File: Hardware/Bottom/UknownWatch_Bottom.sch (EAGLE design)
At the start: 32 parts, among them U1 AD5242-SO16

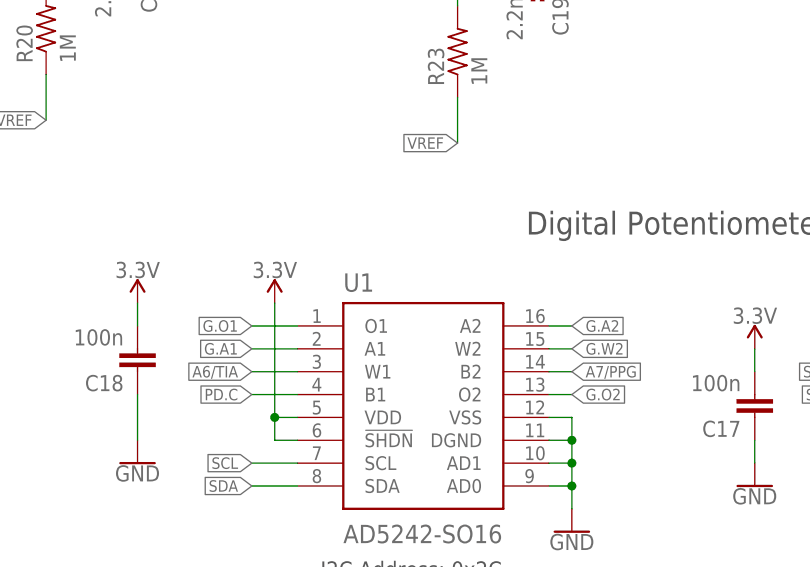
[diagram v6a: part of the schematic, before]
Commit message: Finished bulk of routing on bottom board
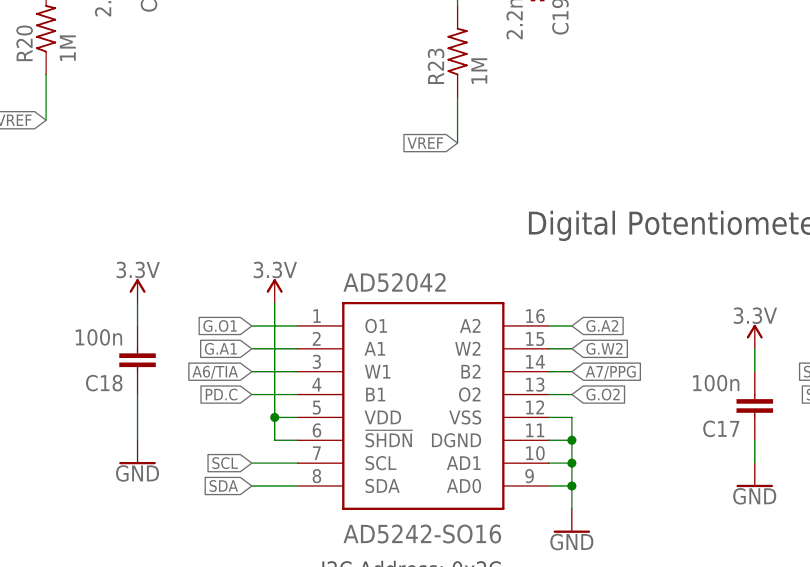
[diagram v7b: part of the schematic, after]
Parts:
- renumbered U1 to AD52042
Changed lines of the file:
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@@
 <part name="GND22" library="LinnesLab-Symbols" deviceset="GND" device=""/>
 <part name="SUPPLY16" library="LinnesLab-Symbols" deviceset="3.3V" device=""/>
-<part name="U1" library="LinnesLab-DigitalIC" deviceset="AD5242" device="-SO16" package3d_urn="urn:adsk.eagle:package:16423/2"/>
+<part name="AD52042" library="LinnesLab-DigitalIC" deviceset="AD5242" device="-SO16" package3d_urn="urn:adsk.eagle:package:16423/2"/>
 <part name="SUPPLY17" library="LinnesLab-Symbols" deviceset="3.3V" device=""/>
 <part name="GND23" library="LinnesLab-Symbols" deviceset="GND" device=""/>
@@
 <attribute name="VALUE" x="106.68" y="38.354" size="1.778" layer="96" align="bottom-center"/>
 </instance>
-<instance part="U1" gate="G$1" x="121.92" y="25.4" smashed="yes">
+<instance part="AD52042" gate="G$1" x="121.92" y="25.4" smashed="yes">
 <attribute name="NAME" x="114.3" y="36.83" size="2.032" layer="95"/>
 <attribute name="VALUE" x="114.3" y="8.89" size="2.032" layer="96"/>
@@
 <wire x1="137.16" y1="15.24" x2="139.7" y2="15.24" width="0.1524" layer="91"/>
 <junction x="139.7" y="15.24"/>
-<pinref part="U1" gate="G$1" pin="VSS"/>
-<pinref part="U1" gate="G$1" pin="DGND"/>
-<pinref part="U1" gate="G$1" pin="AD1"/>
-<pinref part="U1" gate="G$1" pin="AD0"/>
+<pinref part="AD52042" gate="G$1" pin="VSS"/>
+<pinref part="AD52042" gate="G$1" pin="DGND"/>
+<pinref part="AD52042" gate="G$1" pin="AD1"/>
+<pinref part="AD52042" gate="G$1" pin="AD0"/>
 </segment>
 <segment>
@@
 <junction x="106.68" y="22.86"/>
 <pinref part="SUPPLY16" gate="G$1" pin="3.3V"/>
-<pinref part="U1" gate="G$1" pin="VDD"/>
-<pinref part="U1" gate="G$1" pin="!SHDN"/>
+<pinref part="AD52042" gate="G$1" pin="VDD"/>
+<pinref part="AD52042" gate="G$1" pin="!SHDN"/>
 </segment>
 <segment>
@@
 <wire x1="109.22" y1="15.24" x2="104.14" y2="15.24" width="0.1524" layer="91"/>
 <label x="104.14" y="15.24" size="1.27" layer="95" rot="R180" xref="yes"/>
-<pinref part="U1" gate="G$1" pin="SDA"/>
+<pinref part="AD52042" gate="G$1" pin="SDA"/>
 </segment>
 <segment>
@@
 <wire x1="109.22" y1="17.78" x2="104.14" y2="17.78" width="0.1524" layer="91"/>
 <label x="104.14" y="17.78" size="1.27" layer="95" rot="R180" xref="yes"/>
-<pinref part="U1" gate="G$1" pin="SCL"/>
+<pinref part="AD52042" gate="G$1" pin="SCL"/>
 </segment>
 <segment>
@@
 <wire x1="109.22" y1="27.94" x2="104.14" y2="27.94" width="0.1524" layer="91"/>
 <label x="104.14" y="27.94" size="1.27" layer="95" rot="R180" xref="yes"/>
-<pinref part="U1" gate="G$1" pin="W1"/>
+<pinref part="AD52042" gate="G$1" pin="W1"/>
 </segment>
 <segment>
@@
 <wire x1="109.22" y1="25.4" x2="104.14" y2="25.4" width="0.1524" layer="91"/>
 <label x="104.14" y="25.4" size="1.27" layer="95" rot="R180" xref="yes"/>
-<pinref part="U1" gate="G$1" pin="B1"/>
+<pinref part="AD52042" gate="G$1" pin="B1"/>
 </segment>
 </net>
@@
 <wire x1="137.16" y1="30.48" x2="139.7" y2="30.48" width="0.1524" layer="91"/>
 <label x="139.7" y="30.48" size="1.27" layer="95" xref="yes"/>
-<pinref part="U1" gate="G$1" pin="W2"/>
+<pinref part="AD52042" gate="G$1" pin="W2"/>
 </segment>
 <segment>
@@
 <wire x1="109.22" y1="30.48" x2="104.14" y2="30.48" width="0.1524" layer="91"/>
 <label x="104.14" y="30.48" size="1.27" layer="95" rot="R180" xref="yes"/>
-<pinref part="U1" gate="G$1" pin="A1"/>
+<pinref part="AD52042" gate="G$1" pin="A1"/>
 </segment>
 </net>
@@
 <wire x1="137.16" y1="33.02" x2="139.7" y2="33.02" width="0.1524" layer="91"/>
 <label x="139.7" y="33.02" size="1.27" layer="95" xref="yes"/>
-<pinref part="U1" gate="G$1" pin="A2"/>
+<pinref part="AD52042" gate="G$1" pin="A2"/>
 </segment>
 </net>
@@
 <wire x1="137.16" y1="25.4" x2="139.7" y2="25.4" width="0.1524" layer="91"/>
 <label x="139.7" y="25.4" size="1.27" layer="95" xref="yes"/>
-<pinref part="U1" gate="G$1" pin="O2"/>
+<pinref part="AD52042" gate="G$1" pin="O2"/>
 </segment>
 </net>
@@
 <wire x1="109.22" y1="33.02" x2="104.14" y2="33.02" width="0.1524" layer="91"/>
 <label x="104.14" y="33.02" size="1.27" layer="95" rot="R180" xref="yes"/>
-<pinref part="U1" gate="G$1" pin="O1"/>
+<pinref part="AD52042" gate="G$1" pin="O1"/>
 </segment>
 </net>
@@
 <wire x1="137.16" y1="27.94" x2="139.7" y2="27.94" width="0.1524" layer="91"/>
 <label x="139.7" y="27.94" size="1.27" layer="95" xref="yes"/>
-<pinref part="U1" gate="G$1" pin="B2"/>
-</segment>
-</net>
+<pinref part="AD52042" gate="G$1" pin="B2"/>
+</segment>
+</net>

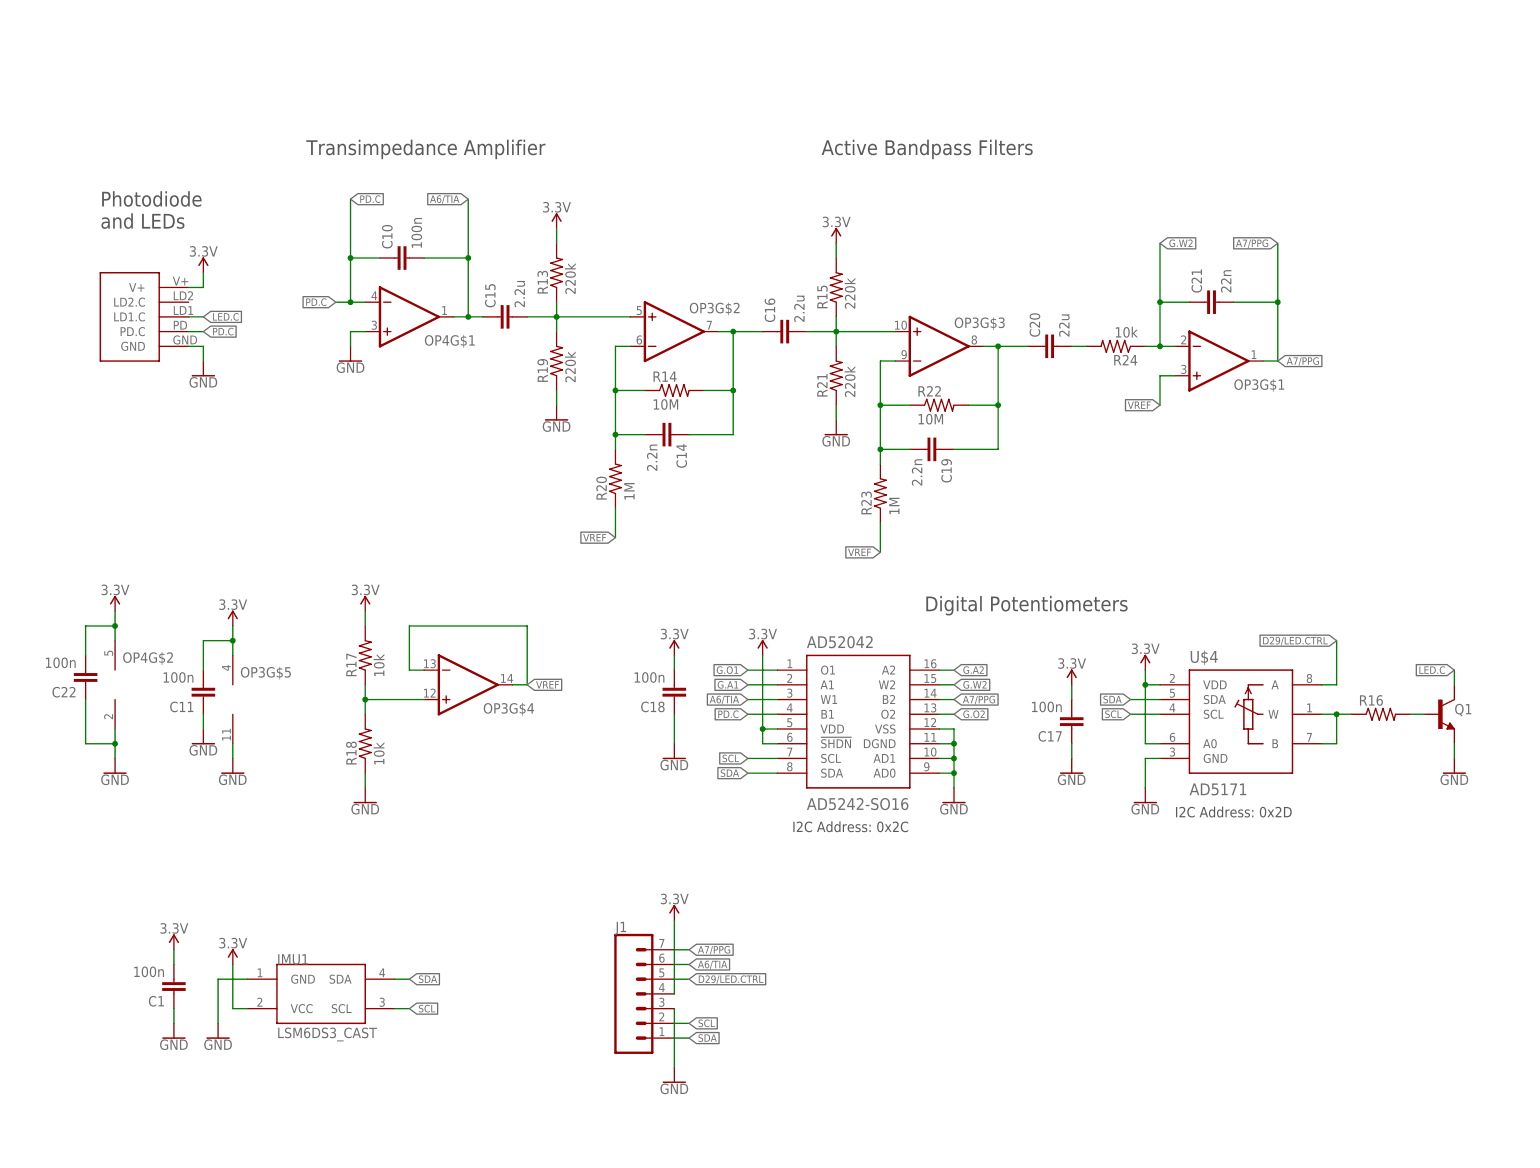
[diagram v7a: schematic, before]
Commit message: Finshed routing the bottom board except for airwire errors
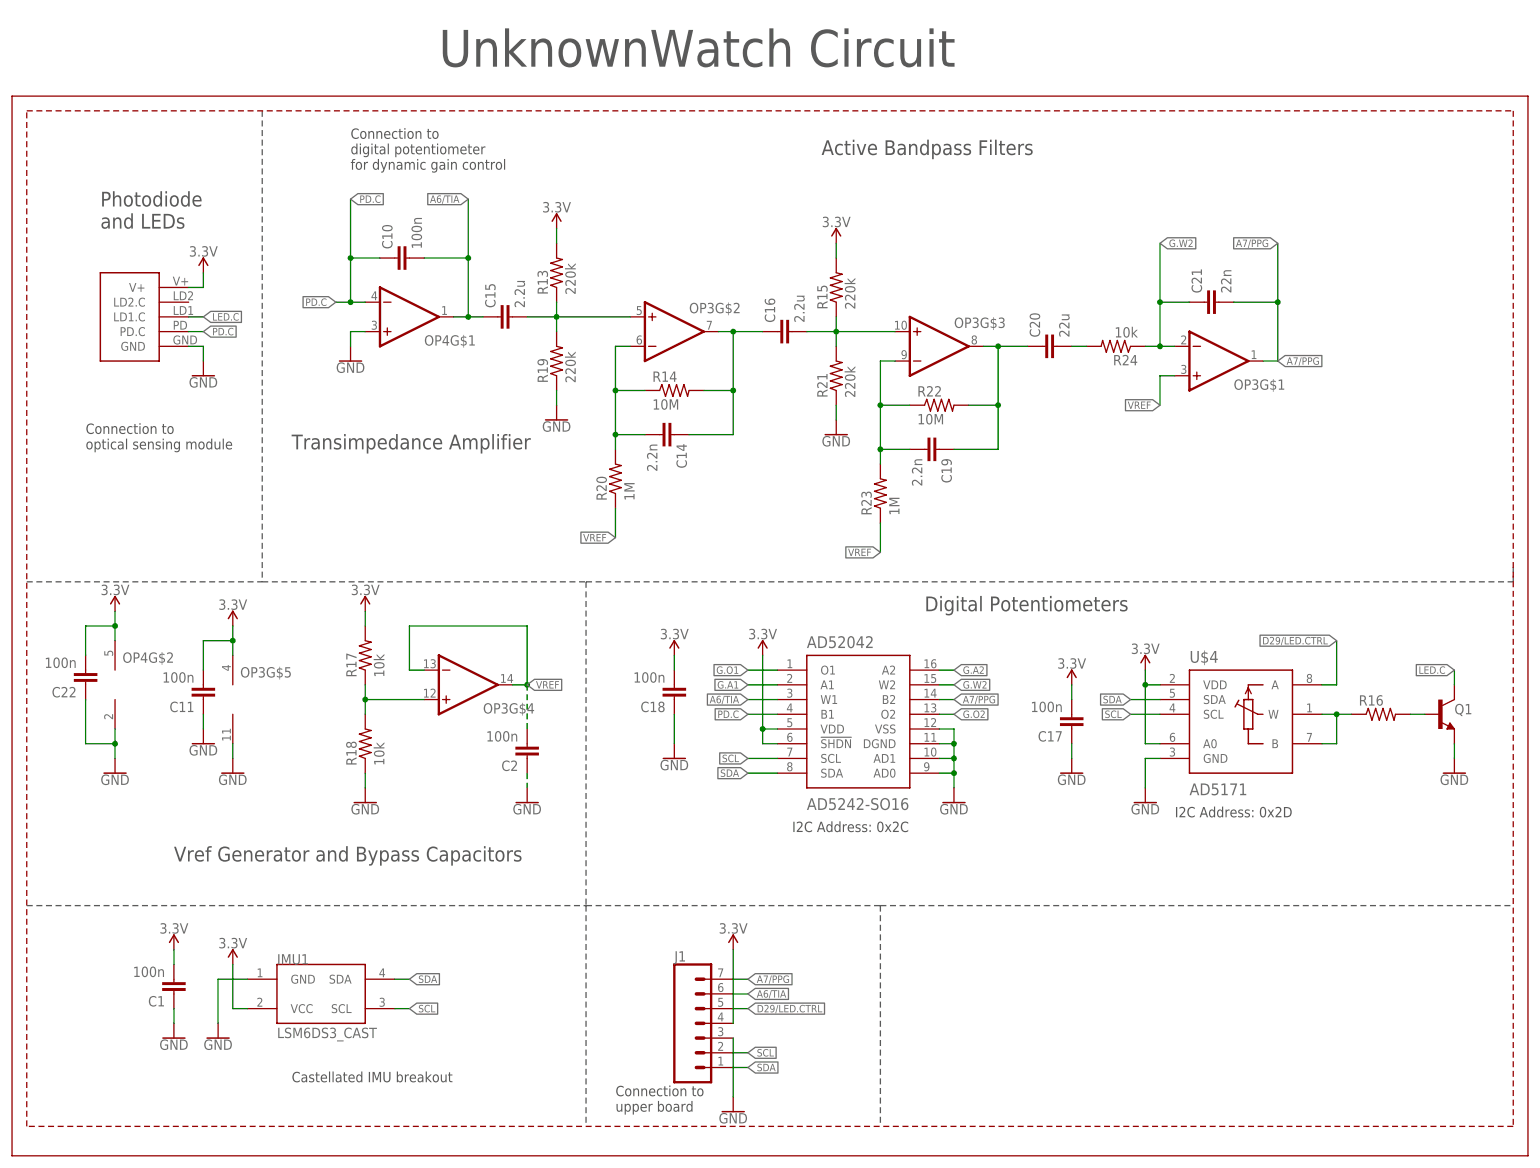
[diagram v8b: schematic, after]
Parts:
- added C2: 100n, LinnesLab-Passives:CAPACITOR0603
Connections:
- net GND: now also C2.1
- net VREF: now also C2.2
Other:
- note added: "Castellated IMU breakout"
- note added: "Connection to digital potentiometer for dynamic gain control"
- note added: "Connection to optical sensing module"
- note added: "Connection to upper board"
- note added: "UnknownWatch Circuit"
- note added: "Vref Generator and Bypass Capacitors"
- moved on the sheet: J1
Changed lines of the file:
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@@
 <part name="GND3" library="LinnesLab-Symbols" deviceset="GND" device=""/>
 <part name="SUPPLY1" library="LinnesLab-Symbols" deviceset="3.3V" device=""/>
+<part name="C2" library="LinnesLab-Passives" deviceset="CAPACITOR" device="0603" value="100n"/>
+<part name="GND5" library="LinnesLab-Symbols" deviceset="GND" device=""/>
 </parts>
 <sheets>
@@
 <text x="116.84" y="121.92" size="2.54" layer="97" font="vector" ratio="15">Active Bandpass Filters</text>
 <text x="134.62" y="43.18" size="2.54" layer="97" font="vector" ratio="15">Digital Potentiometers</text>
-<text x="27.94" y="121.92" size="2.54" layer="97" font="vector" ratio="15">Transimpedance Amplifier</text>
+<text x="25.4" y="71.12" size="2.54" layer="97" font="vector" ratio="15">Transimpedance Amplifier</text>
 <text x="111.76" y="5.08" size="1.778" layer="97" ratio="15">I2C Address: 0x2C</text>
 <text x="177.8" y="7.62" size="1.778" layer="97" ratio="15">I2C Address: 0x2D</text>
+<wire x1="-22.86" y1="132.08" x2="-22.86" y2="-50.8" width="0.1524" layer="94"/>
+<wire x1="-22.86" y1="-50.8" x2="238.76" y2="-50.8" width="0.1524" layer="94"/>
+<wire x1="238.76" y1="-50.8" x2="238.76" y2="132.08" width="0.1524" layer="94"/>
+<wire x1="238.76" y1="132.08" x2="-22.86" y2="132.08" width="0.1524" layer="94"/>
+<wire x1="-20.32" y1="129.54" x2="236.22" y2="129.54" width="0.1524" layer="94" style="longdash"/>
+<wire x1="236.22" y1="129.54" x2="236.22" y2="-45.72" width="0.1524" layer="94" style="longdash"/>
+<wire x1="236.22" y1="-45.72" x2="-20.32" y2="-45.72" width="0.1524" layer="94" style="longdash"/>
+<wire x1="-20.32" y1="-45.72" x2="-20.32" y2="129.54" width="0.1524" layer="94" style="longdash"/>
+<wire x1="-20.32" y1="48.26" x2="20.32" y2="48.26" width="0.1524" layer="97" style="longdash"/>
+<wire x1="20.32" y1="48.26" x2="76.2" y2="48.26" width="0.1524" layer="97" style="longdash"/>
+<wire x1="76.2" y1="48.26" x2="236.22" y2="48.26" width="0.1524" layer="97" style="longdash"/>
+<wire x1="236.22" y1="48.26" x2="236.22" y2="50.8" width="0.1524" layer="97" style="longdash"/>
+<wire x1="76.2" y1="48.26" x2="76.2" y2="-7.62" width="0.1524" layer="97" style="longdash"/>
+<wire x1="76.2" y1="-7.62" x2="76.2" y2="-45.72" width="0.1524" layer="97" style="longdash"/>
+<wire x1="-20.32" y1="-7.62" x2="76.2" y2="-7.62" width="0.1524" layer="97" style="longdash"/>
+<wire x1="76.2" y1="-7.62" x2="127" y2="-7.62" width="0.1524" layer="97" style="longdash"/>
+<wire x1="127" y1="-7.62" x2="236.22" y2="-7.62" width="0.1524" layer="97" style="longdash"/>
+<wire x1="127" y1="-7.62" x2="127" y2="-45.72" width="0.1524" layer="97" style="longdash"/>
+<wire x1="20.32" y1="129.54" x2="20.32" y2="48.26" width="0.1524" layer="97" style="longdash"/>
+<text x="5.08" y="0" size="2.54" layer="97">Vref Generator and Bypass Capacitors</text>
+<text x="-10.16" y="71.12" size="1.778" layer="97">Connection to
+optical sensing module</text>
+<text x="35.56" y="119.38" size="1.778" layer="97">Connection to
+digital potentiometer
+for dynamic gain control</text>
+<text x="81.28" y="-43.18" size="1.778" layer="97">Connection to
+upper board</text>
+<text x="25.4" y="-38.1" size="1.778" layer="97">Castellated IMU breakout</text>
+<text x="50.8" y="137.16" size="6.35" layer="97">UnknownWatch Circuit</text>
 </plain>
 <instances>
@@
 <attribute name="VALUE" x="5.08" y="-12.446" size="1.778" layer="96" align="bottom-center"/>
 </instance>
-<instance part="J1" gate="G$1" x="86.36" y="-25.4" smashed="yes">
-<attribute name="VALUE" x="81.28" y="-35.306" size="1.778" layer="96" font="vector"/>
-<attribute name="NAME" x="81.28" y="-12.192" size="1.778" layer="95" font="vector"/>
-</instance>
-<instance part="GND3" gate="G$1" x="91.44" y="-38.1" smashed="yes">
-<attribute name="VALUE" x="91.44" y="-38.354" size="1.778" layer="96" align="top-center"/>
-</instance>
-<instance part="SUPPLY1" gate="G$1" x="91.44" y="-10.16" smashed="yes">
-<attribute name="VALUE" x="91.44" y="-7.366" size="1.778" layer="96" align="bottom-center"/>
+<instance part="J1" gate="G$1" x="96.52" y="-30.48" smashed="yes">
+<attribute name="VALUE" x="91.44" y="-40.386" size="1.778" layer="96" font="vector"/>
+<attribute name="NAME" x="91.44" y="-17.272" size="1.778" layer="95" font="vector"/>
+</instance>
+<instance part="GND3" gate="G$1" x="101.6" y="-43.18" smashed="yes">
+<attribute name="VALUE" x="101.6" y="-43.434" size="1.778" layer="96" align="top-center"/>
+</instance>
+<instance part="SUPPLY1" gate="G$1" x="101.6" y="-15.24" smashed="yes">
+<attribute name="VALUE" x="101.6" y="-12.446" size="1.778" layer="96" align="bottom-center"/>
+</instance>
+<instance part="C2" gate="G$1" x="66.04" y="20.32" smashed="yes" rot="R180">
+<attribute name="NAME" x="64.516" y="17.399" size="1.778" layer="95" rot="R180"/>
+<attribute name="VALUE" x="64.516" y="22.479" size="1.778" layer="96" rot="R180"/>
+</instance>
+<instance part="GND5" gate="G$1" x="66.04" y="10.16" smashed="yes">
+<attribute name="VALUE" x="66.04" y="9.906" size="1.778" layer="96" align="top-center"/>
 </instance>
 </instances>
@@
 <pinref part="J1" gate="G$1" pin="3"/>
 <pinref part="GND3" gate="G$1" pin="GND"/>
-<wire x1="91.44" y1="-25.4" x2="91.44" y2="-35.56" width="0.1524" layer="91"/>
+<wire x1="101.6" y1="-30.48" x2="101.6" y2="-40.64" width="0.1524" layer="91"/>
+</segment>
+<segment>
+<pinref part="C2" gate="G$1" pin="1"/>
+<pinref part="GND5" gate="G$1" pin="GND"/>
+<wire x1="66.04" y1="15.24" x2="66.04" y2="12.7" width="0.1524" layer="91" style="longdash"/>
 </segment>
 </net>
@@
 <pinref part="J1" gate="G$1" pin="4"/>
 <pinref part="SUPPLY1" gate="G$1" pin="3.3V"/>
-<wire x1="91.44" y1="-22.86" x2="91.44" y2="-10.16" width="0.1524" layer="91"/>
+<wire x1="101.6" y1="-27.94" x2="101.6" y2="-15.24" width="0.1524" layer="91"/>
 </segment>
 </net>
@@
 <segment>
 <pinref part="J1" gate="G$1" pin="1"/>
-<wire x1="91.44" y1="-30.48" x2="93.98" y2="-30.48" width="0.1524" layer="91"/>
-<label x="93.98" y="-30.48" size="1.27" layer="95" xref="yes"/>
+<wire x1="101.6" y1="-35.56" x2="104.14" y2="-35.56" width="0.1524" layer="91"/>
+<label x="104.14" y="-35.56" size="1.27" layer="95" xref="yes"/>
 </segment>
 </net>
@@
 <segment>
 <pinref part="J1" gate="G$1" pin="2"/>
-<wire x1="91.44" y1="-27.94" x2="93.98" y2="-27.94" width="0.1524" layer="91"/>
-<label x="93.98" y="-27.94" size="1.27" layer="95" xref="yes"/>
+<wire x1="101.6" y1="-33.02" x2="104.14" y2="-33.02" width="0.1524" layer="91"/>
+<label x="104.14" y="-33.02" size="1.27" layer="95" xref="yes"/>
 </segment>
 </net>
@@
 <segment>
 <pinref part="J1" gate="G$1" pin="6"/>
-<wire x1="91.44" y1="-17.78" x2="93.98" y2="-17.78" width="0.1524" layer="91"/>
-<label x="93.98" y="-17.78" size="1.27" layer="95" xref="yes"/>
+<wire x1="101.6" y1="-22.86" x2="104.14" y2="-22.86" width="0.1524" layer="91"/>
+<label x="104.14" y="-22.86" size="1.27" layer="95" xref="yes"/>
 </segment>
 </net>
@@
 <wire x1="66.04" y1="30.48" x2="63.5" y2="30.48" width="0.1524" layer="91"/>
 <label x="66.04" y="30.48" size="1.27" layer="95" xref="yes"/>
+<pinref part="C2" gate="G$1" pin="2"/>
+<wire x1="66.04" y1="22.86" x2="66.04" y2="30.48" width="0.1524" layer="91" style="longdash"/>
+<junction x="66.04" y="30.48"/>
 </segment>
 <segment>
@@
 <segment>
 <pinref part="J1" gate="G$1" pin="5"/>
-<wire x1="91.44" y1="-20.32" x2="93.98" y2="-20.32" width="0.1524" layer="91"/>
-<label x="93.98" y="-20.32" size="1.27" layer="95" xref="yes"/>
+<wire x1="101.6" y1="-25.4" x2="104.14" y2="-25.4" width="0.1524" layer="91"/>
+<label x="104.14" y="-25.4" size="1.27" layer="95" xref="yes"/>
 </segment>
 </net>
@@
 <segment>
 <pinref part="J1" gate="G$1" pin="7"/>
-<wire x1="91.44" y1="-15.24" x2="93.98" y2="-15.24" width="0.1524" layer="91"/>
-<label x="93.98" y="-15.24" size="1.27" layer="95" xref="yes"/>
-</segment>
-<segment>
+<wire x1="101.6" y1="-20.32" x2="104.14" y2="-20.32" width="0.1524" layer="91"/>
+<label x="104.14" y="-20.32" size="1.27" layer="95" xref="yes"/>
+</segment>
+<segment>
